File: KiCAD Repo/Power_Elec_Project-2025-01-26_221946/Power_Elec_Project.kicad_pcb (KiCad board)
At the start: 2 copper layers, 3 parts, among them U1 LM358, U2 LAUNCHXL-F28379D

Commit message: PCB layout GD and LPF
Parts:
- removed U1: LM358, Package_SO:VSSOP-8_3x3mm_P0.65mm
- added C1: 0.1uF, Capacitor_SMD:C_0603_1608Metric, F.Cu at (117.0, 108.0)
- added C10: 1.5 µF, Capacitor_SMD:C_0805_2012Metric, B.Cu at (110.1, 121.9)
- added C11: 10uF, Capacitor_SMD:C_0603_1608Metric, F.Cu at (126.0, 108.0)
- added C12: 0.1uF, Capacitor_SMD:C_0603_1608Metric, F.Cu at (126.0, 118.0)
- added C13: 22uF, Capacitor_SMD:C_0603_1608Metric, F.Cu at (126.0, 120.0)
- added C14: 0.1uF, Capacitor_SMD:C_0603_1608Metric, F.Cu at (118.0, 122.0)
- added C2: 1.5 µF, Capacitor_SMD:C_0805_2012Metric, B.Cu at (124.0, 129.0)
- added C3: 33pF, Capacitor_SMD:C_0603_1608Metric, F.Cu at (103.5, 106.0)
- added C4: 2.2uF, Capacitor_SMD:C_0805_2012Metric, F.Cu at (100.0, 106.5)
- added C5: 1.5 µF, Capacitor_SMD:C_0805_2012Metric, B.Cu at (110.1, 109.9)
- added C6: 2.2uF, Capacitor_SMD:C_0805_2012Metric, F.Cu at (100.5, 122.5)
- added C7: 10uF, Capacitor_SMD:C_0603_1608Metric, F.Cu at (100.5, 126.0)
- added C8: 10uF, Capacitor_SMD:C_0603_1608Metric, F.Cu at (100.5, 124.5)
- added C9: 0.1uF, Capacitor_SMD:C_0603_1608Metric, F.Cu at (126.0, 110.0)
- added D1: US2AA, Diode_SMD:D_SMA, F.Cu at (102.5, 132.0)
- added D2: ISO 12V, LED_SMD:LED_0603_1608Metric, F.Cu at (91.0, 119.5)
- added D3: MCU 5V, LED_SMD:LED_0603_1608Metric, F.Cu at (90.7, 108.0)
- added D4: ISO 3.3v, LED_SMD:LED_0603_1608Metric, F.Cu at (135.0, 119.5)
- added D5: MCU 3.3v, LED_SMD:LED_0603_1608Metric, F.Cu at (135.0, 107.0)
- added L1: 18mH, Inductor_THT:L_Radial_D12.0mm_P6.00mm_Murata_1900R, F.Cu at (120.5, 132.5)
- added PS1: R05C1TF05S-R, R05C1TF05S-R:CONV_R05C1TF05S-R, F.Cu at (127.0, 114.0)
- added R10: 50, Resistor_SMD:R_0603_1608Metric, B.Cu at (136.0, 120.0)
- added R11: 50, Resistor_SMD:R_0603_1608Metric, B.Cu at (135.5, 122.0)
- added R12: 12, Resistor_SMD:R_0805_2012Metric_Pad1.20x1.40mm_HandSolder, B.Cu at (132.5, 120.0)
- added R13: 12, Resistor_SMD:R_0805_2012Metric_Pad1.20x1.40mm_HandSolder, B.Cu at (132.5, 109.5)
- added R14: 50, Resistor_SMD:R_0603_1608Metric, B.Cu at (136.0, 109.5)
- added R15: 50, Resistor_SMD:R_0603_1608Metric, B.Cu at (136.0, 107.5)
- added R2: 16.2k, Resistor_SMD:R_0603_1608Metric, B.Cu at (123.0, 132.0)
- added R3: 50, Resistor_SMD:R_0603_1608Metric, F.Cu at (105.5, 106.5)
- added R4: 12, Resistor_SMD:R_0805_2012Metric_Pad1.20x1.40mm_HandSolder, F.Cu at (104.5, 128.3)
- added R5: 50, Resistor_SMD:R_0603_1608Metric, F.Cu at (99.5, 128.5)
- added R6: 7, Resistor_SMD:R_0603_1608Metric, F.Cu at (101.5, 128.5)
- added R7: 1.8k, Resistor_SMD:R_0603_1608Metric, B.Cu at (91.0, 119.0)
- added R8: 1.8k, Resistor_SMD:R_0603_1608Metric, B.Cu at (90.7, 107.0)
- added R9: 1.8k, Resistor_SMD:R_0603_1608Metric, B.Cu at (90.7, 109.0)
- added U3: UCC5304DWVR, UCC5304DWVR GateDriver_IC:SOIC8_DWV_TEX, F.Cu at (102.0, 114.5)
- added U4: TMV 0512SHI, TMV_0512SHI:TMV-HI_SINGLE_TRP, F.Cu at (112.6, 108.8)
- added U5: AMC1300DWVR, Opamp AMC1300DWVR:DWV8_TEX, F.Cu at (121.0, 114.0)
- R1: value 10k -> 165; footprint Resistor_SMD:R_0805_2012Metric -> Resistor_SMD:R_0603_1608Metric
- moved R1 65.4 mm to (121.5, 122.0)
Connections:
- R1 pad 2: unconnected-(R1-Pad2) -> GNDPWR

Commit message: PCB layout
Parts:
- moved C11 20.9 mm to (110.5, 122.0)
- moved C12 20.9 mm to (110.5, 132.0)
- moved C13 20.9 mm to (110.5, 134.0)
- moved C14 20.9 mm to (102.5, 136.0)
- moved C2 20.9 mm to (108.5, 143.0)
- moved C9 20.9 mm to (110.5, 124.0)
- moved D4 20.9 mm to (119.5, 133.5)
- moved D5 20.9 mm to (119.5, 121.0)
- moved L1 20.9 mm to (105.0, 146.5)
- moved PS1 20.9 mm to (111.5, 128.0)
- moved R1 20.9 mm to (106.0, 136.0)
- moved R10 20.9 mm to (120.5, 134.0)
- moved R11 20.9 mm to (120.0, 136.0)
- moved R12 20.9 mm to (117.0, 134.0)
- moved R13 20.9 mm to (117.0, 123.5)
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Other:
- board outline added: 131.5 x 93 mm

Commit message: PCB
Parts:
- added C15: 470uF, Capacitor_THT:CP_Radial_D10.0mm_P5.00mm, F.Cu at (144.5, 144.4)
- added C16: 1uF, Capacitor_SMD:C_1206_3216Metric_Pad1.33x1.80mm_HandSolder, F.Cu at (213.5, 124.9)
- added C17: 2.2uF, Capacitor_THT:CP_Radial_D8.0mm_P3.50mm, F.Cu at (204.0, 123.5)
- added D6: SS310, Diode_SMD:D_SMA, F.Cu at (214.6, 121.0)
- added J1: RED, Connector:Banana_Jack_1Pin, F.Cu at (160.5, 144.0)
- added J2: RED, Connector:Banana_Jack_1Pin, F.Cu at (194.5, 102.8)
- added J3: RED, Connector:Banana_Jack_1Pin, F.Cu at (194.5, 115.4)
- added J4: Black, Connector:Banana_Jack_1Pin, F.Cu at (194.5, 128.0)
- added J5: Black, Connector:Banana_Jack_1Pin, F.Cu at (194.5, 140.5)
- added L2: 2.2mH, Barrel Inductor AIRD-06-182K:AIRD-06_ABR, F.Cu at (204.2, 95.6)
- added Q1: IRF540N, Package_TO_SOT_THT:TO-220-3_Vertical, F.Cu at (215.8, 111.1)
- R2: value 16.2k -> 20.5k
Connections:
- U2 pad J10_2: unconnected-(U2I-GND_J10-PadJ10_2) -> GND
- U2 pad J10_3: unconnected-(U2I-GND_J10__1-PadJ10_3) -> GND
- U2 pad J12_3: unconnected-(U2J-GND_J12-PadJ12_3) -> GND
- U2 pad J14_5: unconnected-(U2K-GND_J14-PadJ14_5) -> GND
- U2 pad J15_5: unconnected-(U2L-GND_J15-PadJ15_5) -> GND
- U2 pad J16_2: unconnected-(U2N-GND_J16-PadJ16_2) -> GND
- U2 pad J16_3: unconnected-(U2N-GND_J16__1-PadJ16_3) -> GND
- U2 pad J1_1: unconnected-(U2A-3.3V_J1-PadJ1_1) -> +3.3V
- U2 pad J21_2: unconnected-(U2M-TP21/GND-PadJ21_2) -> GND
- U2 pad J21_4: unconnected-(U2M-TP22/GND-PadJ21_4) -> GND
- U2 pad J21_6: unconnected-(U2M-TP23/GND-PadJ21_6) -> GND
- U2 pad J21_8: unconnected-(U2M-TP24/GND-PadJ21_8) -> GND
- U2 pad J2_10: unconnected-(U2B-GND_J2-PadJ2_10) -> GND
- U2 pad J3_2: unconnected-(U2C-GND_J3-PadJ3_2) -> GND
- U2 pad J3_3: unconnected-(U2C-ADCIN14/ANALOGIN-PadJ3_3) -> /VFILT
- U2 pad J7_1: unconnected-(U2G-+5V_J7-PadJ7_1) -> +5V
- U2 pad J7_2: unconnected-(U2G-GND_J7-PadJ7_2) -> GND
- U2 pad J8_5: unconnected-(U2H-GPIO11/PWMOUT6B-PadJ8_5) -> /PWM

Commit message: PCB
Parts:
- moved C16 131.6 mm to (82.0, 119.5), turned to -90 degrees
- moved Q1 113.8 mm to (102.0, 112.0), turned to -90 degrees
- moved D6 112.2 mm to (102.5, 125.0), turned to -90 degrees
- moved J4 109.2 mm to (85.5, 134.5)
- moved L2 96.6 mm to (110.6, 120.0)
- moved J1 84.3 mm to (85.5, 105.5)
- moved C17 69.1 mm to (135.0, 128.0), turned to -90 degrees
- moved D2 62.2 mm to (132.5, 107.5)
- moved R7 62.2 mm to (132.5, 107.0)
- moved C15 60.9 mm to (90.0, 117.1), turned to -90 degrees
- moved C1 60.3 mm to (158.5, 101.0)
- moved C11 60.3 mm to (167.0, 101.0)
- moved C12 60.3 mm to (167.0, 111.0)
- moved C13 60.3 mm to (167.0, 113.0)
- moved C14 60.3 mm to (159.0, 115.0)
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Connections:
- C15 pad 2: Net-(D6-A) -> GNDPWR
- C16 pad 2: Net-(D6-A) -> GNDPWR
- C17 pad 2: Net-(D6-A) -> GNDPWR
- D6 pad 2: Net-(D6-A) -> GNDPWR
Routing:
- net +3.3V: track 0.00 -> 92.7 mm, vias 0 -> 1
- net GND: track 0.00 -> 86.6 mm, vias 0 -> 246
- net /PWM: track 0.00 -> 70.9 mm, vias 0 -> 2
- net +5V: track 0.00 -> 62.8 mm, vias 0 -> 1
- net GNDREF: track 0.00 -> 60.6 mm, vias 0 -> 39
- net /VFILT: track 0.00 -> 60.0 mm
- net /VG: track 0.00 -> 50.4 mm
- net ISO_12V: track 0.00 -> 39.4 mm, vias 0 -> 1
- net ISO_3.3V: track 0.00 -> 33.9 mm, vias 0 -> 2
- net Net-(U5-INP): track 0.00 -> 14.1 mm, vias 0 -> 1
- net GNDPWR: track 0.00 -> 13.6 mm, vias 0 -> 94
- net /VOUT: track 0.00 -> 6.61 mm, vias 0 -> 38
- net Net-(D4-A): track 0.00 -> 6.04 mm, vias 0 -> 1
- net Net-(D3-A): track 0.00 -> 5.68 mm, vias 0 -> 1
- net Net-(C2-Pad1): track 0.00 -> 5.24 mm
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- added copper zone on B.Cu, net /VOUT
- added copper zone on F.Cu, net /VOUT
- added copper zone on B.Cu, net GND
- added copper zone on F.Cu, net GND
- added copper zone on B.Cu, net GNDPWR
- added copper zone on F.Cu, net GNDPWR
- added copper zone on B.Cu, net GNDREF
- added copper zone on F.Cu, net GNDREF
- added copper zone on B.Cu, net VDD
- added copper zone on F.Cu, net VDD
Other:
- board size 131.5 x 93 mm -> 131.5 x 105.7 mm

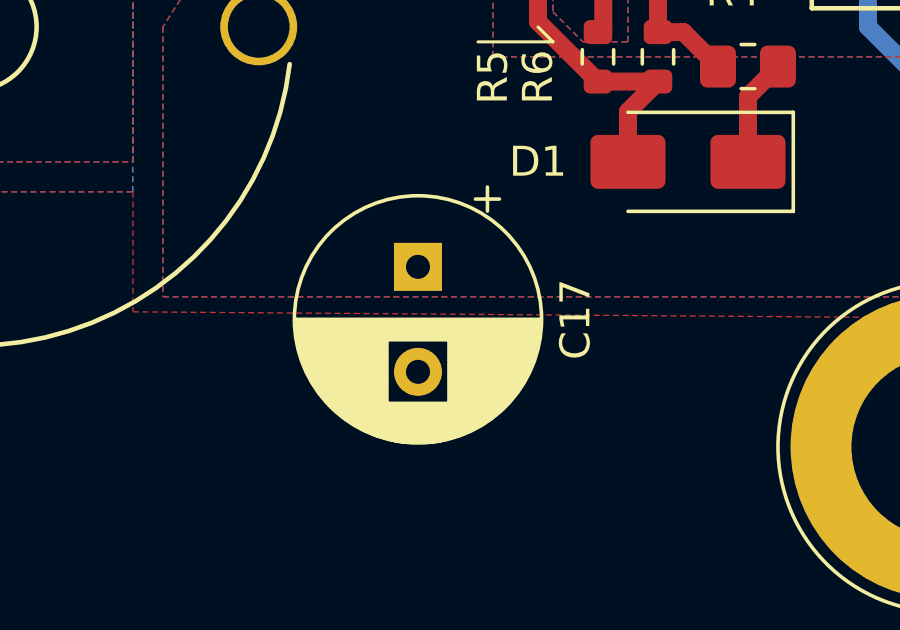
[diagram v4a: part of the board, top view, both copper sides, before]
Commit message: Capacitor change
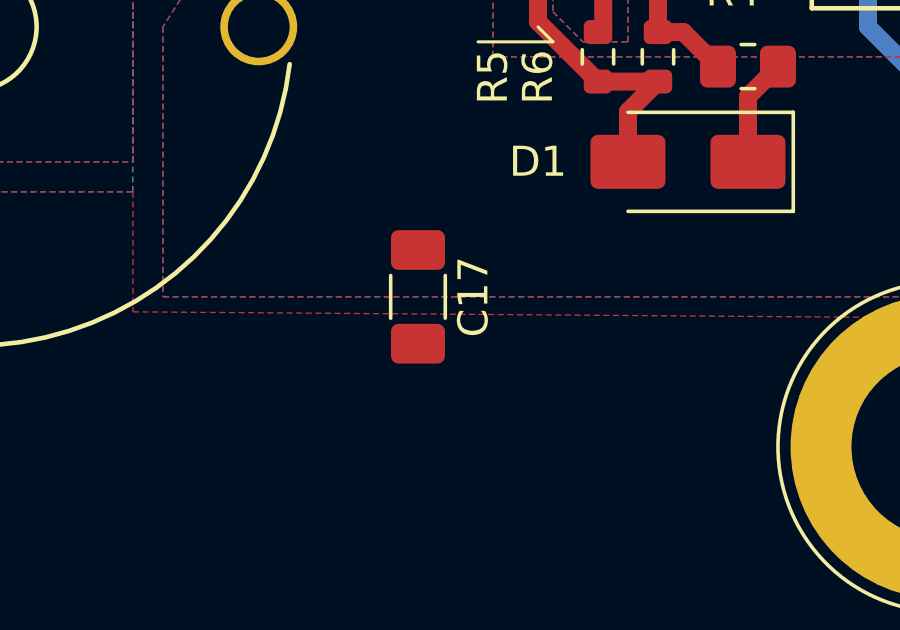
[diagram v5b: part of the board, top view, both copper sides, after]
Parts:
- C17: value 2.2uF -> 4.7uF; footprint Capacitor_THT:CP_Radial_D8.0mm_P3.50mm -> Capacitor_SMD:C_1206_3216Metric_Pad1.33x1.80mm_HandSolder
- moved C17 1.00 mm to (135.0, 129.0)

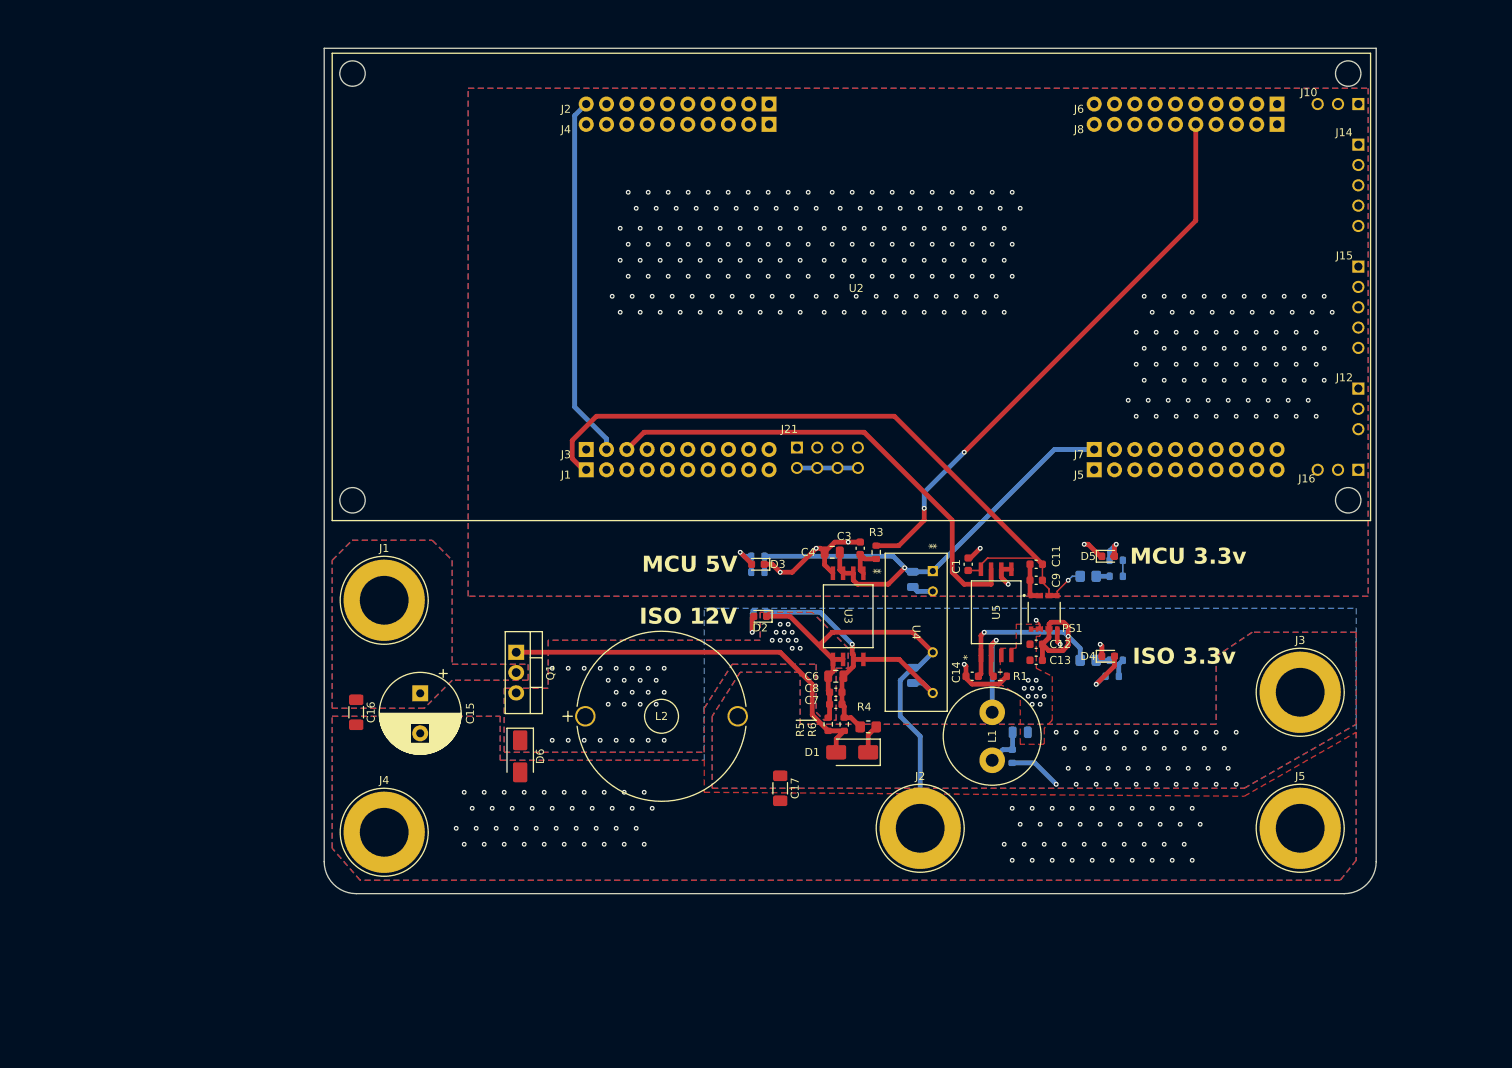
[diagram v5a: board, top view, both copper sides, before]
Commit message: Inductor and PCB fix
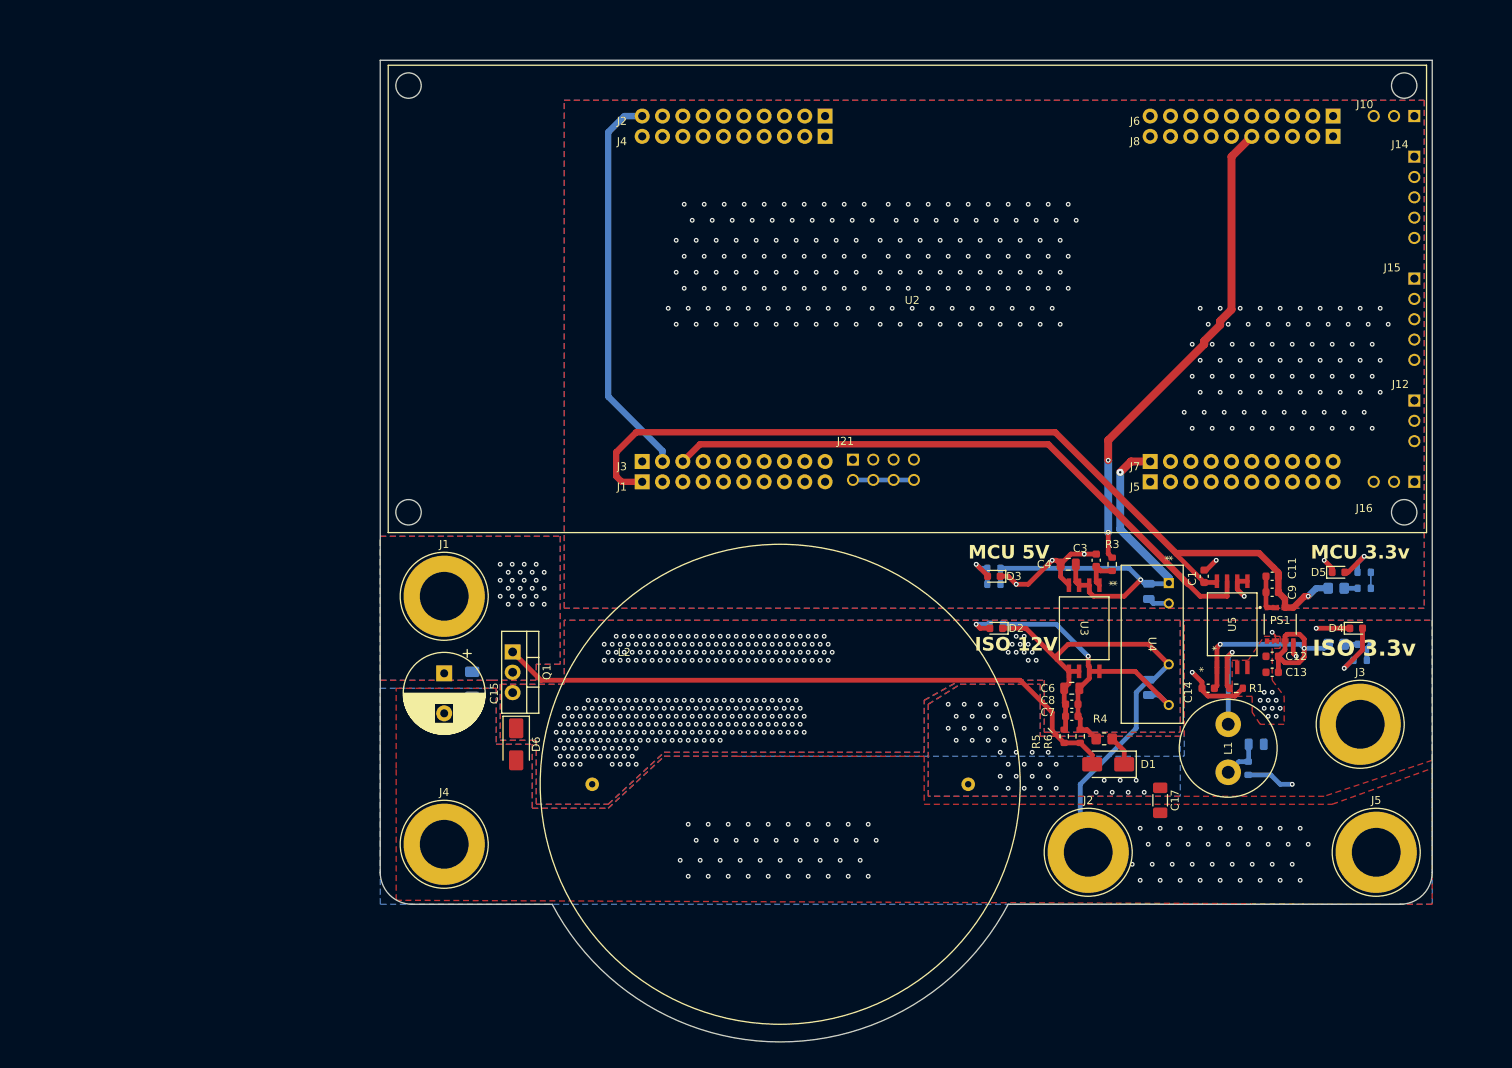
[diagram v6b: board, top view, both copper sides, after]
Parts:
- C16: moved to B.Cu
- L2: value 2.2mH -> 68mH; footprint Barrel Inductor AIRD-06-182K:AIRD-06_ABR -> CustomLIB:Inductor_Throughhole_Radial; D=60mm, P=47mm
- moved C17 47.5 mm to (182.5, 130.5)
- moved D1 32.0 mm to (176.0, 126.0)
- moved D4 31.2 mm to (207.0, 109.0)
- moved R10 31.1 mm to (208.0, 111.0)
- moved R11 31.1 mm to (207.5, 113.0)
- moved R12 31.1 mm to (204.5, 111.0)
- moved R13 31.0 mm to (204.5, 104.0)
- moved R14 31.0 mm to (208.0, 104.0)
- moved R15 31.0 mm to (208.0, 102.0)
- moved C1 29.5 mm to (188.0, 102.5)
- moved C10 29.5 mm to (181.1, 116.4)
- moved C11 29.5 mm to (196.5, 102.5)
- moved C12 29.5 mm to (196.5, 112.5)
- moved C13 29.5 mm to (196.5, 114.5)
- moved C14 29.5 mm to (188.5, 116.5)
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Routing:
- net /VG: track 50.4 -> 80.3 mm
- net +3.3V: track 92.7 -> 115.6 mm
- net /VFILT: track 60.0 -> 78.7 mm
- net /PWM: track 70.9 -> 60.3 mm
- net +5V: track 62.8 -> 57.0 mm, vias 1 -> 2
- net GNDPWR: track 13.6 -> 17.2 mm, vias 94 -> 90
- net GND: track 86.6 -> 89.5 mm
- net GNDREF: track 60.6 -> 63.5 mm, vias 39 -> 326
- net Net-(D4-A): track 6.04 -> 7.54 mm
- net Net-(D5-A): track 4.22 -> 5.60 mm
- net Net-(D2-A): track 4.66 -> 3.59 mm
- net /VOUT: track 6.61 -> 5.99 mm, vias 38 -> 40
- net VDD: vias 0 -> 24
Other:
- board size 131.5 x 105.7 mm -> 131.5 x 122.7 mm

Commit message: PCB fix
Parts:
- added H1: MountingHole, MountingHole:MountingHole_2.2mm_M2, F.Cu at (102.0, 139.5)
- added H3: MountingHole, MountingHole:MountingHole_2.2mm_M2, F.Cu at (199.0, 140.0)
- added H5: MountingHole, MountingHole:MountingHole_2.2mm_M2, F.Cu at (88.0, 35.5)
- added H7: MountingHole, MountingHole:MountingHole_2.2mm_M2, F.Cu at (213.5, 35.5)
- added HS1: Heatsink, Heatsink:Heatsink_Stonecold_HS-S03_13.21x12.7mm, B.Cu at (98.5, 114.5)
- moved C15 2.00 mm to (91.0, 114.6)
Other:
- board size 131.5 x 122.7 mm -> 131.5 x 128.2 mm

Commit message: PCB fix
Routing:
- net GNDPWR: track 17.2 -> 16.7 mm
- net /VOUT: vias 40 -> 43
